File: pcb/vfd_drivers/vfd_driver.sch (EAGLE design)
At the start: 5 parts

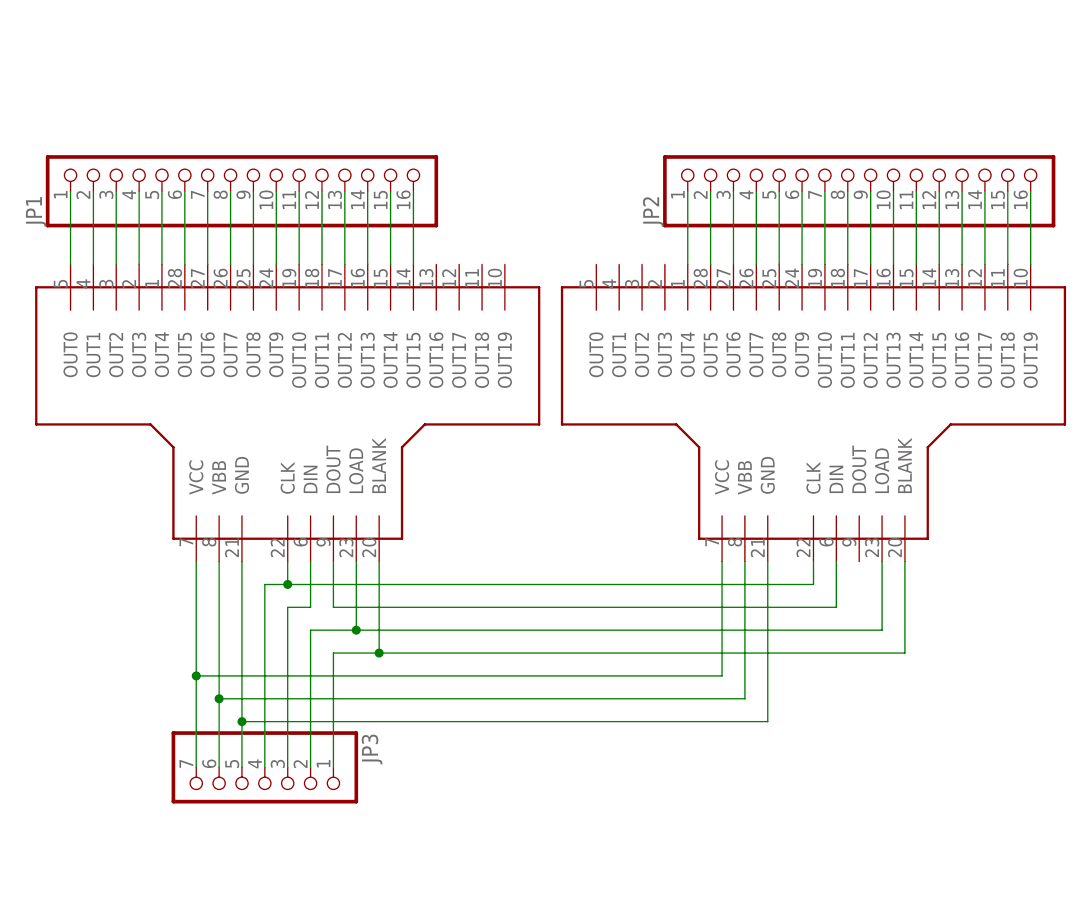
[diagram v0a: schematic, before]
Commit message: Finalized the VFD driver carrier board
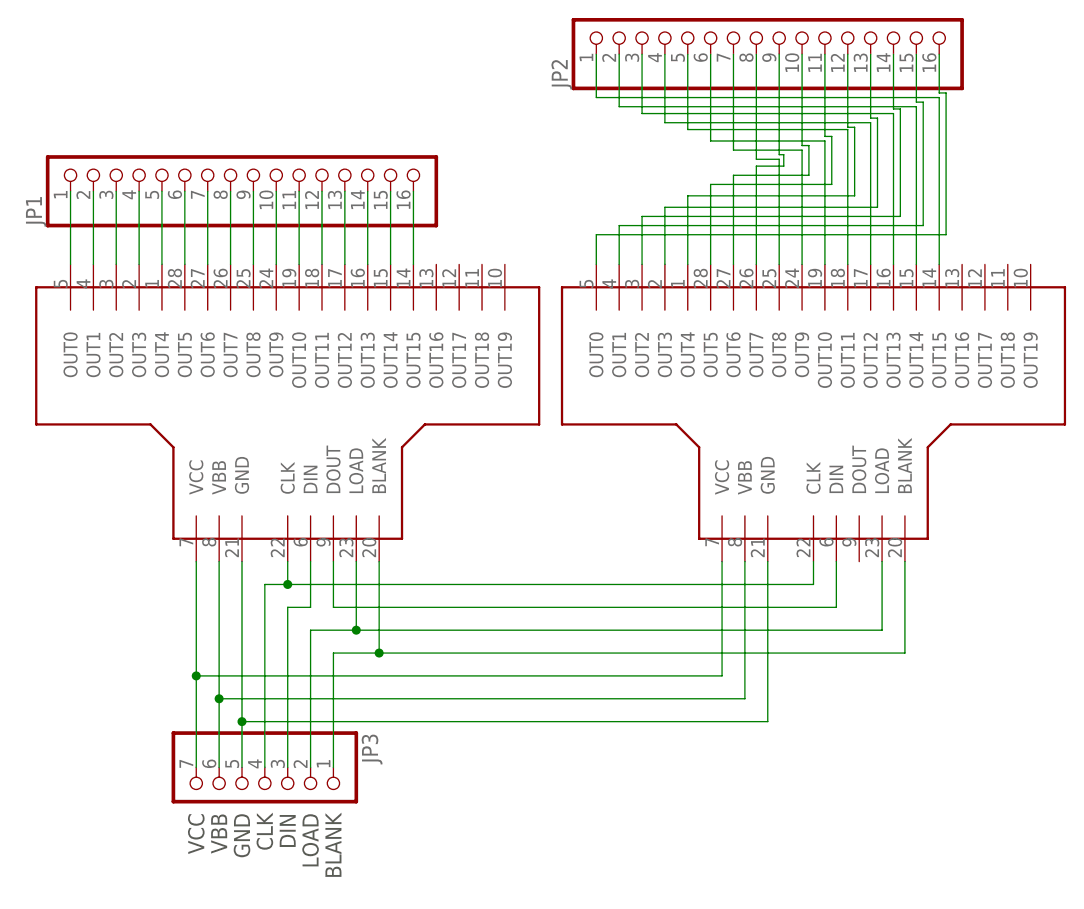
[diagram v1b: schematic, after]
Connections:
- removed net N$17: JP2.9, U$2.OUT12
- removed net N$18: JP2.8, U$2.OUT11
- removed net N$19: JP2.7, U$2.OUT10
- removed net N$20: JP2.6, U$2.OUT9
- removed net N$21: JP2.5, U$2.OUT8
- removed net N$22: JP2.4, U$2.OUT7
- removed net N$23: JP2.3, U$2.OUT6
- removed net N$24: JP2.2, U$2.OUT5
- removed net N$25: JP2.1, U$2.OUT4
- new net N$1: JP2.1, U$2.OUT15
- new net N$2: JP2.2, U$2.OUT14
- new net N$3: JP2.3, U$2.OUT13
- new net N$4: JP2.4, U$2.OUT12
- new net N$5: JP2.5, U$2.OUT11
- new net N$6: JP2.6, U$2.OUT10
- new net N$7: JP2.7, U$2.OUT9
- new net N$8: JP2.8, U$2.OUT8
- new net N$9: JP2.9, U$2.OUT7
- net N$10: now also JP2.10, U$2.OUT6; no longer JP2.16, U$2.OUT19
- net N$11: now also JP2.11, U$2.OUT5; no longer JP2.15, U$2.OUT18
- net N$12: now also JP2.12, U$2.OUT4; no longer JP2.14, U$2.OUT17
- net N$13: now also U$2.OUT3; no longer U$2.OUT16
- net N$14: now also JP2.14, U$2.OUT2; no longer JP2.12, U$2.OUT15
- net N$15: now also JP2.15, U$2.OUT1; no longer JP2.11, U$2.OUT14
- net N$16: now also JP2.16, U$2.OUT0; no longer JP2.10, U$2.OUT13
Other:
- note added: "BLANK"
- note added: "CLK"
- note added: "DIN"
- note added: "GND"
- note added: "LOAD"
- note added: "VBB"
- note added: "VCC"
- moved on the sheet: JP2
